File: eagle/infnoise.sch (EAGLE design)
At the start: 25 parts, among them SW1 NS5B1G385DFT2G, SW2 NS5B1G385DFT2G, U1 FT240XQ, X1 USBSMT-MALE

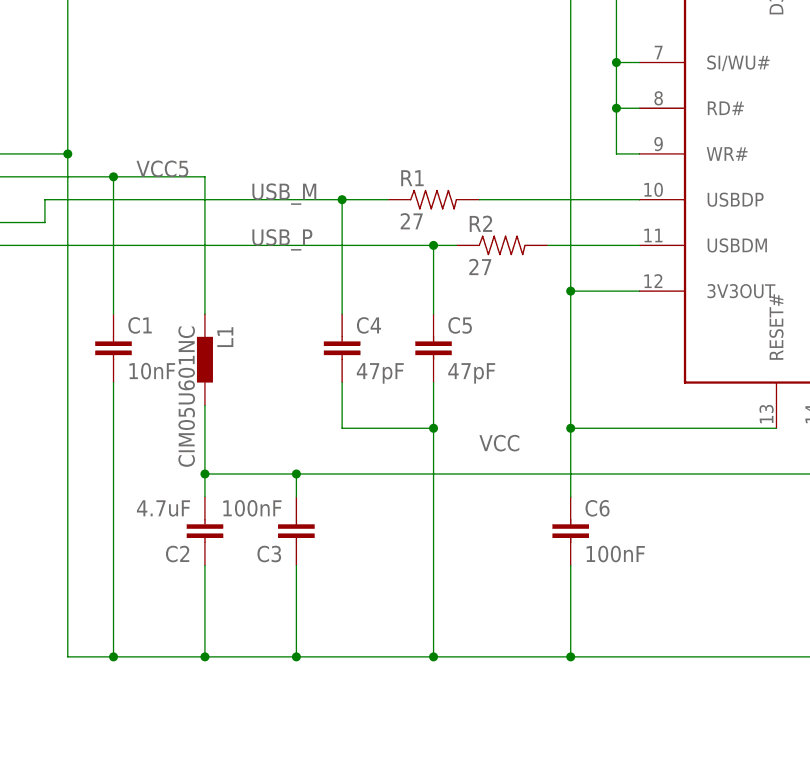
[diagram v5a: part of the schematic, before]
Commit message: Converted to 0603 parts to be compatible with Small Batch Assembly
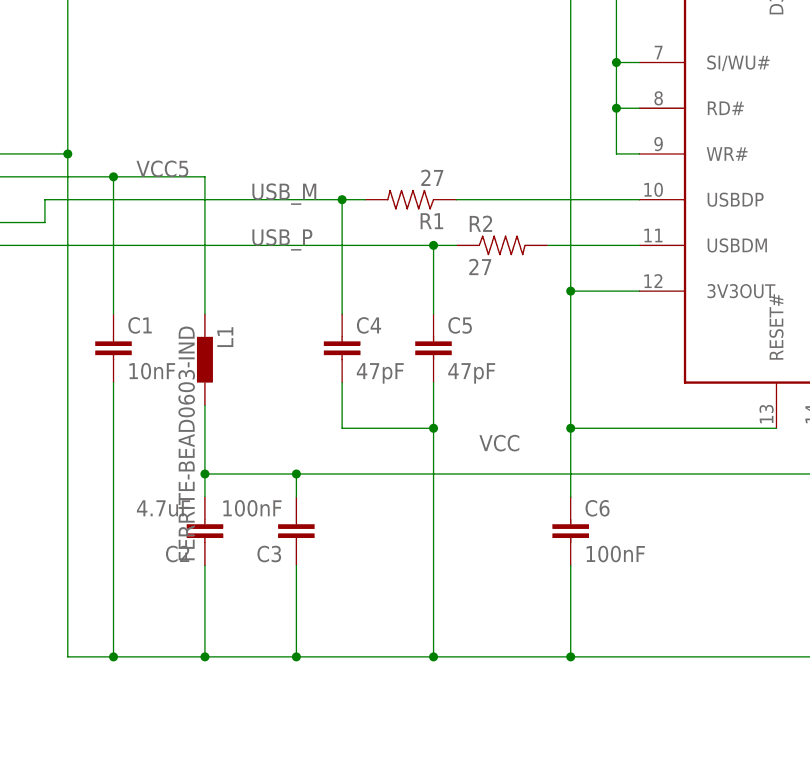
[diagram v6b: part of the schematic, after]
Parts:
- C1, C3, C4, C5, C6, C7, C8: device infnoise:CAP0402-CAP -> infnoise:CAP0603-CAP
- L1: value CIM05U601NC -> FERRITE-BEAD0603-IND; device infnoise:CIM05U601NC -> infnoise:FERRITE-BEAD0603-IND
- R1, R10, R2, R3, R4, R5, R6, R7, R8, R9: device infnoise:RESISTOR0402-RES -> infnoise:RESISTOR0603-RES
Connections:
- removed net USBDP: R1.2, U1.USBDP
- new net N$2: R1.1, U1.USBDP
- net USB_M: now also R1.2; no longer R1.1
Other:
- moved on the sheet: R1
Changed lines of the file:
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@@
 <grid distance="0.1" unitdist="inch" unit="inch" style="lines" multiple="1" display="no" altdistance="0.01" altunitdist="inch" altunit="inch"/>
 <layers>
-<layer number="1" name="Top" color="4" fill="1" visible="yes" active="no"/>
-<layer number="16" name="Bottom" color="1" fill="1" visible="yes" active="no"/>
-<layer number="17" name="Pads" color="2" fill="1" visible="yes" active="no"/>
-<layer number="18" name="Vias" color="2" fill="1" visible="yes" active="no"/>
-<layer number="19" name="Unrouted" color="6" fill="1" visible="yes" active="no"/>
-<layer number="20" name="Dimension" color="15" fill="1" visible="yes" active="no"/>
-<layer number="21" name="tPlace" color="7" fill="1" visible="yes" active="no"/>
-<layer number="22" name="bPlace" color="7" fill="1" visible="yes" active="no"/>
-<layer number="23" name="tOrigins" color="15" fill="1" visible="yes" active="no"/>
-<layer number="24" name="bOrigins" color="15" fill="1" visible="yes" active="no"/>
-<layer number="25" name="tNames" color="7" fill="1" visible="yes" active="no"/>
-<layer number="26" name="bNames" color="7" fill="1" visible="yes" active="no"/>
-<layer number="27" name="tValues" color="7" fill="1" visible="yes" active="no"/>
-<layer number="28" name="bValues" color="7" fill="1" visible="yes" active="no"/>
+<layer number="1" name="Top" color="4" fill="1" visible="no" active="no"/>
+<layer number="16" name="Bottom" color="1" fill="1" visible="no" active="no"/>
+<layer number="17" name="Pads" color="2" fill="1" visible="no" active="no"/>
+<layer number="18" name="Vias" color="2" fill="1" visible="no" active="no"/>
+<layer number="19" name="Unrouted" color="6" fill="1" visible="no" active="no"/>
+<layer number="20" name="Dimension" color="15" fill="1" visible="no" active="no"/>
+<layer number="21" name="tPlace" color="7" fill="1" visible="no" active="no"/>
+<layer number="22" name="bPlace" color="7" fill="1" visible="no" active="no"/>
+<layer number="23" name="tOrigins" color="15" fill="1" visible="no" active="no"/>
+<layer number="24" name="bOrigins" color="15" fill="1" visible="no" active="no"/>
+<layer number="25" name="tNames" color="7" fill="1" visible="no" active="no"/>
+<layer number="26" name="bNames" color="7" fill="1" visible="no" active="no"/>
+<layer number="27" name="tValues" color="7" fill="1" visible="no" active="no"/>
+<layer number="28" name="bValues" color="7" fill="1" visible="no" active="no"/>
 <layer number="29" name="tStop" color="7" fill="3" visible="no" active="no"/>
 <layer number="30" name="bStop" color="7" fill="6" visible="no" active="no"/>
@@
 <layer number="35" name="tGlue" color="7" fill="4" visible="no" active="no"/>
 <layer number="36" name="bGlue" color="7" fill="5" visible="no" active="no"/>
-<layer number="37" name="tTest" color="7" fill="1" visible="yes" active="no"/>
-<layer number="38" name="bTest" color="7" fill="1" visible="yes" active="no"/>
+<layer number="37" name="tTest" color="7" fill="1" visible="no" active="no"/>
+<layer number="38" name="bTest" color="7" fill="1" visible="no" active="no"/>
 <layer number="39" name="tKeepout" color="4" fill="11" visible="no" active="no"/>
 <layer number="40" name="bKeepout" color="1" fill="11" visible="no" active="no"/>
@@
 <layer number="44" name="Drills" color="7" fill="1" visible="no" active="no"/>
 <layer number="45" name="Holes" color="7" fill="1" visible="no" active="no"/>
-<layer number="46" name="Milling" color="3" fill="1" visible="yes" active="no"/>
-<layer number="47" name="Measures" color="7" fill="1" visible="yes" active="no"/>
-<layer number="48" name="Document" color="7" fill="1" visible="yes" active="no"/>
-<layer number="49" name="Reference" color="7" fill="1" visible="yes" active="no"/>
-<layer number="51" name="tDocu" color="7" fill="1" visible="yes" active="no"/>
-<layer number="52" name="bDocu" color="7" fill="1" visible="yes" active="no"/>
+<layer number="46" name="Milling" color="3" fill="1" visible="no" active="no"/>
+<layer number="47" name="Measures" color="7" fill="1" visible="no" active="no"/>
+<layer number="48" name="Document" color="7" fill="1" visible="no" active="no"/>
+<layer number="49" name="Reference" color="7" fill="1" visible="no" active="no"/>
+<layer number="51" name="tDocu" color="7" fill="1" visible="no" active="no"/>
+<layer number="52" name="bDocu" color="7" fill="1" visible="no" active="no"/>
 <layer number="90" name="Modules" color="5" fill="1" visible="yes" active="yes"/>
 <layer number="91" name="Nets" color="2" fill="1" visible="yes" active="yes"/>
@@
 <parts>
 <part name="U1" library="infnoise" deviceset="FT240X" device="Q"/>
-<part name="C4" library="infnoise" deviceset="CAP" device="0402-CAP" value="47pF"/>
-<part name="C5" library="infnoise" deviceset="CAP" device="0402-CAP" value="47pF"/>
-<part name="C6" library="infnoise" deviceset="CAP" device="0402-CAP" value="100nF"/>
+<part name="C4" library="infnoise" deviceset="CAP" device="0603-CAP" value="47pF"/>
+<part name="C5" library="infnoise" deviceset="CAP" device="0603-CAP" value="47pF"/>
+<part name="C6" library="infnoise" deviceset="CAP" device="0603-CAP" value="100nF"/>
 <part name="C2" library="infnoise" deviceset="CAP" device="0603-CAP" value="4.7uF"/>
-<part name="C3" library="infnoise" deviceset="CAP" device="0402-CAP" value="100nF"/>
-<part name="C7" library="infnoise" deviceset="CAP" device="0402-CAP" value="100pF"/>
-<part name="C8" library="infnoise" deviceset="CAP" device="0402-CAP" value="100pF"/>
-<part name="C1" library="infnoise" deviceset="CAP" device="0402-CAP" value="10nF"/>
-<part name="L1" library="infnoise" deviceset="CIM05U601NC" device=""/>
-<part name="R1" library="infnoise" deviceset="RESISTOR" device="0402-RES" value="27"/>
-<part name="R2" library="infnoise" deviceset="RESISTOR" device="0402-RES" value="27"/>
-<part name="R6" library="infnoise" deviceset="RESISTOR" device="0402-RES" value="8.2K"/>
-<part name="R5" library="infnoise" deviceset="RESISTOR" device="0402-RES" value="10K"/>
-<part name="R7" library="infnoise" deviceset="RESISTOR" device="0402-RES" value="8.2K"/>
-<part name="R8" library="infnoise" deviceset="RESISTOR" device="0402-RES" value="10K"/>
-<part name="R3" library="infnoise" deviceset="RESISTOR" device="0402-RES" value="10K"/>
-<part name="R4" library="infnoise" deviceset="RESISTOR" device="0402-RES" value="10K"/>
+<part name="C3" library="infnoise" deviceset="CAP" device="0603-CAP" value="100nF"/>
+<part name="C7" library="infnoise" deviceset="CAP" device="0603-CAP" value="100pF"/>
+<part name="C8" library="infnoise" deviceset="CAP" device="0603-CAP" value="100pF"/>
+<part name="C1" library="infnoise" deviceset="CAP" device="0603-CAP" value="10nF"/>
+<part name="L1" library="infnoise" deviceset="FERRITE-BEAD" device="0603-IND"/>
+<part name="R1" library="infnoise" deviceset="RESISTOR" device="0603-RES" value="27"/>
+<part name="R2" library="infnoise" deviceset="RESISTOR" device="0603-RES" value="27"/>
+<part name="R6" library="infnoise" deviceset="RESISTOR" device="0603-RES" value="8.2K"/>
+<part name="R5" library="infnoise" deviceset="RESISTOR" device="0603-RES" value="10K"/>
+<part name="R7" library="infnoise" deviceset="RESISTOR" device="0603-RES" value="8.2K"/>
+<part name="R8" library="infnoise" deviceset="RESISTOR" device="0603-RES" value="10K"/>
+<part name="R3" library="infnoise" deviceset="RESISTOR" device="0603-RES" value="10K"/>
+<part name="R4" library="infnoise" deviceset="RESISTOR" device="0603-RES" value="10K"/>
 <part name="AMP" library="infnoise" deviceset="TSV912" device="IQ2T"/>
 <part name="CMP" library="infnoise" deviceset="TC75W57" device="FK"/>
 <part name="SUPPLY1" library="supply2" deviceset="GND" device=""/>
-<part name="R9" library="infnoise" deviceset="RESISTOR" device="0402-RES" value="8.2K"/>
-<part name="R10" library="infnoise" deviceset="RESISTOR" device="0402-RES" value="8.2K"/>
+<part name="R9" library="infnoise" deviceset="RESISTOR" device="0603-RES" value="8.2K"/>
+<part name="R10" library="infnoise" deviceset="RESISTOR" device="0603-RES" value="8.2K"/>
 <part name="SW1" library="infnoise" deviceset="NS5B1G385" device="DFT2G"/>
 <part name="SW2" library="infnoise" deviceset="NS5B1G385" device="DFT2G"/>
@@
 <instance part="C1" gate="G$1" x="-20.32" y="17.78"/>
 <instance part="L1" gate="G$1" x="-10.16" y="17.78" rot="R270"/>
-<instance part="R1" gate="G$1" x="15.24" y="35.56"/>
+<instance part="R1" gate="G$1" x="12.7" y="35.56" rot="R180"/>
 <instance part="R2" gate="G$1" x="22.86" y="30.48"/>
 <instance part="R6" gate="G$1" x="172.72" y="60.96"/>
@@
 </busses>
 <nets>
-<net name="USBDP" class="0">
-<segment>
-<pinref part="R1" gate="G$1" pin="2"/>
-<pinref part="U1" gate="G$1" pin="USBDP"/>
-<wire x1="20.32" y1="35.56" x2="38.1" y2="35.56" width="0.1524" layer="91"/>
-</segment>
-</net>
 <net name="USB_M" class="0">
 <segment>
-<pinref part="R1" gate="G$1" pin="1"/>
-<wire x1="10.16" y1="35.56" x2="5.08" y2="35.56" width="0.1524" layer="91"/>
 <wire x1="5.08" y1="35.56" x2="-27.94" y2="35.56" width="0.1524" layer="91"/>
 <wire x1="-27.94" y1="35.56" x2="-27.94" y2="33.02" width="0.1524" layer="91"/>
@@
 <wire x1="5.08" y1="22.86" x2="5.08" y2="35.56" width="0.1524" layer="91"/>
 <label x="-5.08" y="35.56" size="1.778" layer="95"/>
+<pinref part="X1" gate="G$1" pin="D+"/>
+<pinref part="R1" gate="G$1" pin="2"/>
+<wire x1="5.08" y1="35.56" x2="7.62" y2="35.56" width="0.1524" layer="91"/>
 <junction x="5.08" y="35.56"/>
-<pinref part="X1" gate="G$1" pin="D+"/>
 </segment>
 </net>
@@
 </segment>
 </net>
+<net name="N$2" class="0">
+<segment>
+<pinref part="R1" gate="G$1" pin="1"/>
+<pinref part="U1" gate="G$1" pin="USBDP"/>
+<wire x1="17.78" y1="35.56" x2="38.1" y2="35.56" width="0.1524" layer="91"/>
+</segment>
+</net>

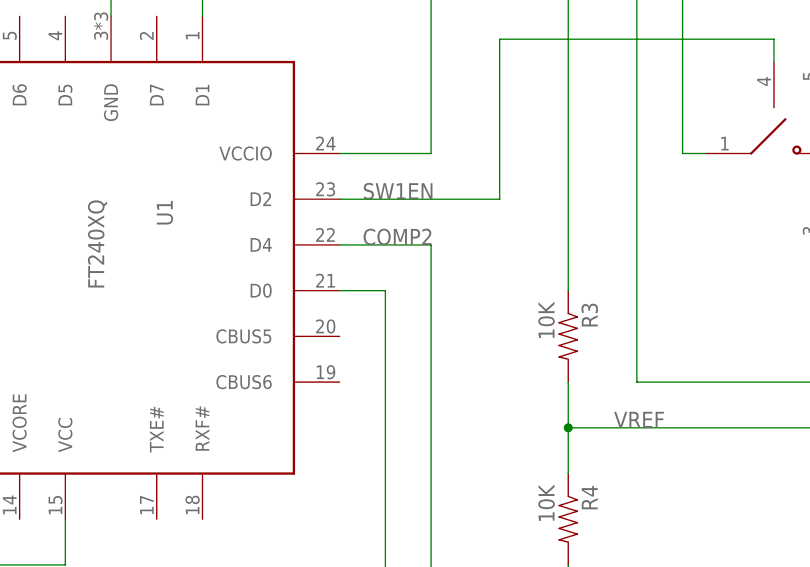
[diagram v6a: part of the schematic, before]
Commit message: Updated driver to use correct pins
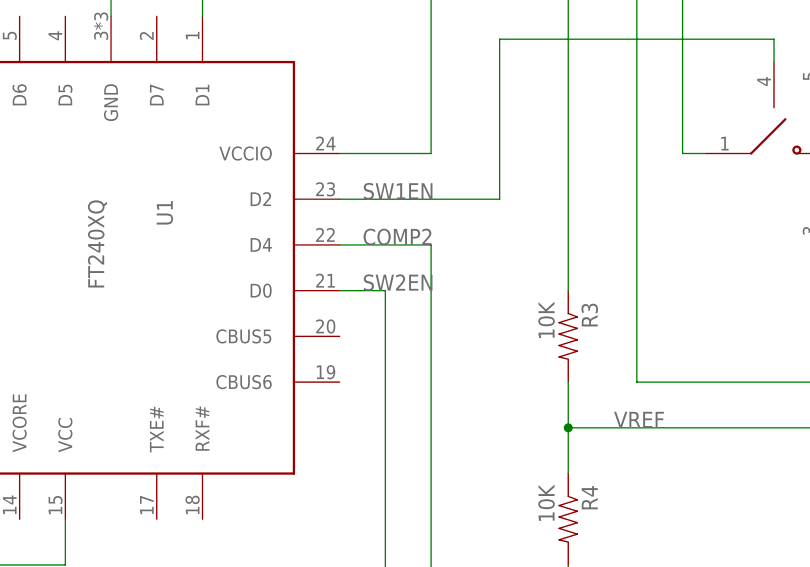
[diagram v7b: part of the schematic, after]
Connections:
- net N$1 renamed SW2EN
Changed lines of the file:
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@@
 </segment>
 </net>
-<net name="N$1" class="0">
+<net name="SW2EN" class="0">
 <segment>
 <pinref part="SW2" gate="G$1" pin="IN"/>
@@
 <pinref part="U1" gate="G$1" pin="D0"/>
 <wire x1="99.06" y1="35.56" x2="93.98" y2="35.56" width="0.1524" layer="91"/>
+<label x="96.52" y="35.56" size="1.778" layer="95"/>
 </segment>
 </net>

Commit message: tweaks
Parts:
- R6, R7: value 8.2K -> 9.76K
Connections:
- removed net VCC5: C1.1, L1.1, X1.VBUS
- new net VCCIN: C1.1, L1.1, X1.VCC
- net USB_M: now also C5.1, R2.1, X1.D-; no longer C4.1, R1.2, X1.D+
- net USB_P: now also C4.1, R1.2, X1.D+; no longer C5.1, R2.1, X1.D-
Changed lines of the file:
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@@
 <layer number="91" name="Nets" color="2" fill="1" visible="yes" active="yes"/>
 <layer number="92" name="Busses" color="1" fill="1" visible="yes" active="yes"/>
-<layer number="93" name="Pins" color="2" fill="1" visible="no" active="yes"/>
+<layer number="93" name="Pins" color="2" fill="1" visible="yes" active="yes"/>
 <layer number="94" name="Symbols" color="4" fill="1" visible="yes" active="yes"/>
 <layer number="95" name="Names" color="7" fill="1" visible="yes" active="yes"/>
@@
 <part name="R1" library="infnoise" deviceset="RESISTOR" device="0603-RES" value="27"/>
 <part name="R2" library="infnoise" deviceset="RESISTOR" device="0603-RES" value="27"/>
-<part name="R6" library="infnoise" deviceset="RESISTOR" device="0603-RES" value="8.2K"/>
+<part name="R6" library="infnoise" deviceset="RESISTOR" device="0603-RES" value="9.76K"/>
 <part name="R5" library="infnoise" deviceset="RESISTOR" device="0603-RES" value="10K"/>
-<part name="R7" library="infnoise" deviceset="RESISTOR" device="0603-RES" value="8.2K"/>
+<part name="R7" library="infnoise" deviceset="RESISTOR" device="0603-RES" value="9.76K"/>
 <part name="R8" library="infnoise" deviceset="RESISTOR" device="0603-RES" value="10K"/>
 <part name="R3" library="infnoise" deviceset="RESISTOR" device="0603-RES" value="10K"/>
@@
 <instance part="SW1" gate="G$1" x="142.24" y="50.8"/>
 <instance part="SW2" gate="G$1" x="281.94" y="45.72" rot="MR0"/>
-<instance part="X1" gate="G$1" x="-43.18" y="40.64" rot="R180"/>
+<instance part="X1" gate="G$1" x="-43.18" y="35.56" rot="R180"/>
 </instances>
 <busses>
 </busses>
 <nets>
-<net name="USB_M" class="0">
-<segment>
-<wire x1="5.08" y1="35.56" x2="-27.94" y2="35.56" width="0.1524" layer="91"/>
-<wire x1="-27.94" y1="35.56" x2="-27.94" y2="33.02" width="0.1524" layer="91"/>
-<wire x1="-27.94" y1="33.02" x2="-40.64" y2="33.02" width="0.1524" layer="91"/>
+<net name="USB_P" class="0">
+<segment>
+<wire x1="5.08" y1="35.56" x2="-12.7" y2="35.56" width="0.1524" layer="91"/>
 <pinref part="C4" gate="G$1" pin="1"/>
 <wire x1="5.08" y1="22.86" x2="5.08" y2="35.56" width="0.1524" layer="91"/>
 <label x="-5.08" y="35.56" size="1.778" layer="95"/>
-<pinref part="X1" gate="G$1" pin="D+"/>
 <pinref part="R1" gate="G$1" pin="2"/>
 <wire x1="5.08" y1="35.56" x2="7.62" y2="35.56" width="0.1524" layer="91"/>
 <junction x="5.08" y="35.56"/>
-</segment>
-</net>
-<net name="USB_P" class="0">
+<wire x1="-12.7" y1="35.56" x2="-12.7" y2="33.02" width="0.1524" layer="91"/>
+<pinref part="X1" gate="G$1" pin="D+"/>
+<wire x1="-12.7" y1="33.02" x2="-40.64" y2="33.02" width="0.1524" layer="91"/>
+</segment>
+</net>
+<net name="USB_M" class="0">
 <segment>
 <pinref part="R2" gate="G$1" pin="1"/>
 <wire x1="17.78" y1="30.48" x2="15.24" y2="30.48" width="0.1524" layer="91"/>
-<wire x1="15.24" y1="30.48" x2="-33.02" y2="30.48" width="0.1524" layer="91"/>
-<wire x1="-33.02" y1="30.48" x2="-33.02" y2="35.56" width="0.1524" layer="91"/>
-<wire x1="-33.02" y1="35.56" x2="-40.64" y2="35.56" width="0.1524" layer="91"/>
+<wire x1="15.24" y1="30.48" x2="-40.64" y2="30.48" width="0.1524" layer="91"/>
 <pinref part="C5" gate="G$1" pin="1"/>
 <wire x1="15.24" y1="22.86" x2="15.24" y2="30.48" width="0.1524" layer="91"/>
@@
 </segment>
 </net>
-<net name="VCC5" class="0">
-<segment>
-<wire x1="-40.64" y1="38.1" x2="-20.32" y2="38.1" width="0.1524" layer="91"/>
-<wire x1="-20.32" y1="38.1" x2="-10.16" y2="38.1" width="0.1524" layer="91"/>
+<net name="VCCIN" class="0">
+<segment>
+<wire x1="-20.32" y1="27.94" x2="-10.16" y2="27.94" width="0.1524" layer="91"/>
 <pinref part="C1" gate="G$1" pin="1"/>
-<wire x1="-20.32" y1="22.86" x2="-20.32" y2="38.1" width="0.1524" layer="91"/>
-<junction x="-20.32" y="38.1"/>
-<label x="-17.78" y="38.1" size="1.778" layer="95"/>
+<wire x1="-20.32" y1="22.86" x2="-20.32" y2="27.94" width="0.1524" layer="91"/>
+<label x="-17.78" y="27.94" size="1.778" layer="95"/>
 <pinref part="L1" gate="G$1" pin="1"/>
-<wire x1="-10.16" y1="22.86" x2="-10.16" y2="38.1" width="0.1524" layer="91"/>
-<pinref part="X1" gate="G$1" pin="VBUS"/>
+<wire x1="-10.16" y1="22.86" x2="-10.16" y2="27.94" width="0.1524" layer="91"/>
+<pinref part="X1" gate="G$1" pin="VCC"/>
+<wire x1="-40.64" y1="27.94" x2="-20.32" y2="27.94" width="0.1524" layer="91"/>
+<junction x="-20.32" y="27.94"/>
 </segment>
 </net>
@@
 <wire x1="63.5" y1="10.16" x2="63.5" y2="5.08" width="0.1524" layer="91"/>
 <wire x1="63.5" y1="5.08" x2="0" y2="5.08" width="0.1524" layer="91"/>
-<label x="20.32" y="7.62" size="1.778" layer="95"/>
+<label x="20.32" y="5.08" size="1.778" layer="95"/>
 <pinref part="C3" gate="G$1" pin="2"/>
 <wire x1="0" y1="5.08" x2="-10.16" y2="5.08" width="0.1524" layer="91"/>
@@
 <pinref part="SUPPLY1" gate="GND" pin="GND"/>
 <wire x1="66.04" y1="-17.78" x2="66.04" y2="-15.24" width="0.1524" layer="91"/>
-<wire x1="-40.64" y1="40.64" x2="-25.4" y2="40.64" width="0.1524" layer="91"/>
-<wire x1="-25.4" y1="40.64" x2="-25.4" y2="-15.24" width="0.1524" layer="91"/>
+<wire x1="-25.4" y1="71.12" x2="-25.4" y2="35.56" width="0.1524" layer="91"/>
+<wire x1="-25.4" y1="35.56" x2="-25.4" y2="-15.24" width="0.1524" layer="91"/>
 <wire x1="-25.4" y1="-15.24" x2="-20.32" y2="-15.24" width="0.1524" layer="91"/>
 <pinref part="C1" gate="G$1" pin="2"/>
@@
 <wire x1="68.58" y1="71.12" x2="35.56" y2="71.12" width="0.1524" layer="91"/>
 <wire x1="35.56" y1="71.12" x2="-25.4" y2="71.12" width="0.1524" layer="91"/>
-<wire x1="-25.4" y1="71.12" x2="-25.4" y2="40.64" width="0.1524" layer="91"/>
 <wire x1="66.04" y1="-15.24" x2="119.38" y2="-15.24" width="0.1524" layer="91"/>
 <wire x1="119.38" y1="-15.24" x2="147.32" y2="-15.24" width="0.1524" layer="91"/>
@@
 <pinref part="SW2" gate="G$1" pin="GND"/>
 <wire x1="276.86" y1="35.56" x2="276.86" y2="-15.24" width="0.1524" layer="91"/>
-<junction x="-25.4" y="40.64"/>
 <junction x="-20.32" y="-15.24"/>
 <junction x="15.24" y="-15.24"/>
@@
 <junction x="119.38" y="-15.24"/>
 <pinref part="X1" gate="G$1" pin="GND"/>
-</segment>
-</net>
+<wire x1="-40.64" y1="35.56" x2="-25.4" y2="35.56" width="0.1524" layer="91"/>
+<junction x="-25.4" y="35.56"/>
+</segment>
+</net>
